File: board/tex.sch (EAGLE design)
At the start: 248 parts, among them K1 HLS8L-DC5V-S-C, K2 HLS8L-DC5V-S-C, K3 HLS8L-DC5V-S-C, K4 HLS8L-DC5V-S-C, Q47 FDD4141, U14 24LC32A, U15 OPTO-LTV817, U16 OPTO-LTV817, U17 OPTO-LTV817, U18 OPTO-LTV817, U19 RELAY-S108T02PTH, U2 RTC-DS1337S, U20 RELAY-S108T02PTH, U21 IO-HC4051, U5 AZ23C5V1, Y1 32.768KHz

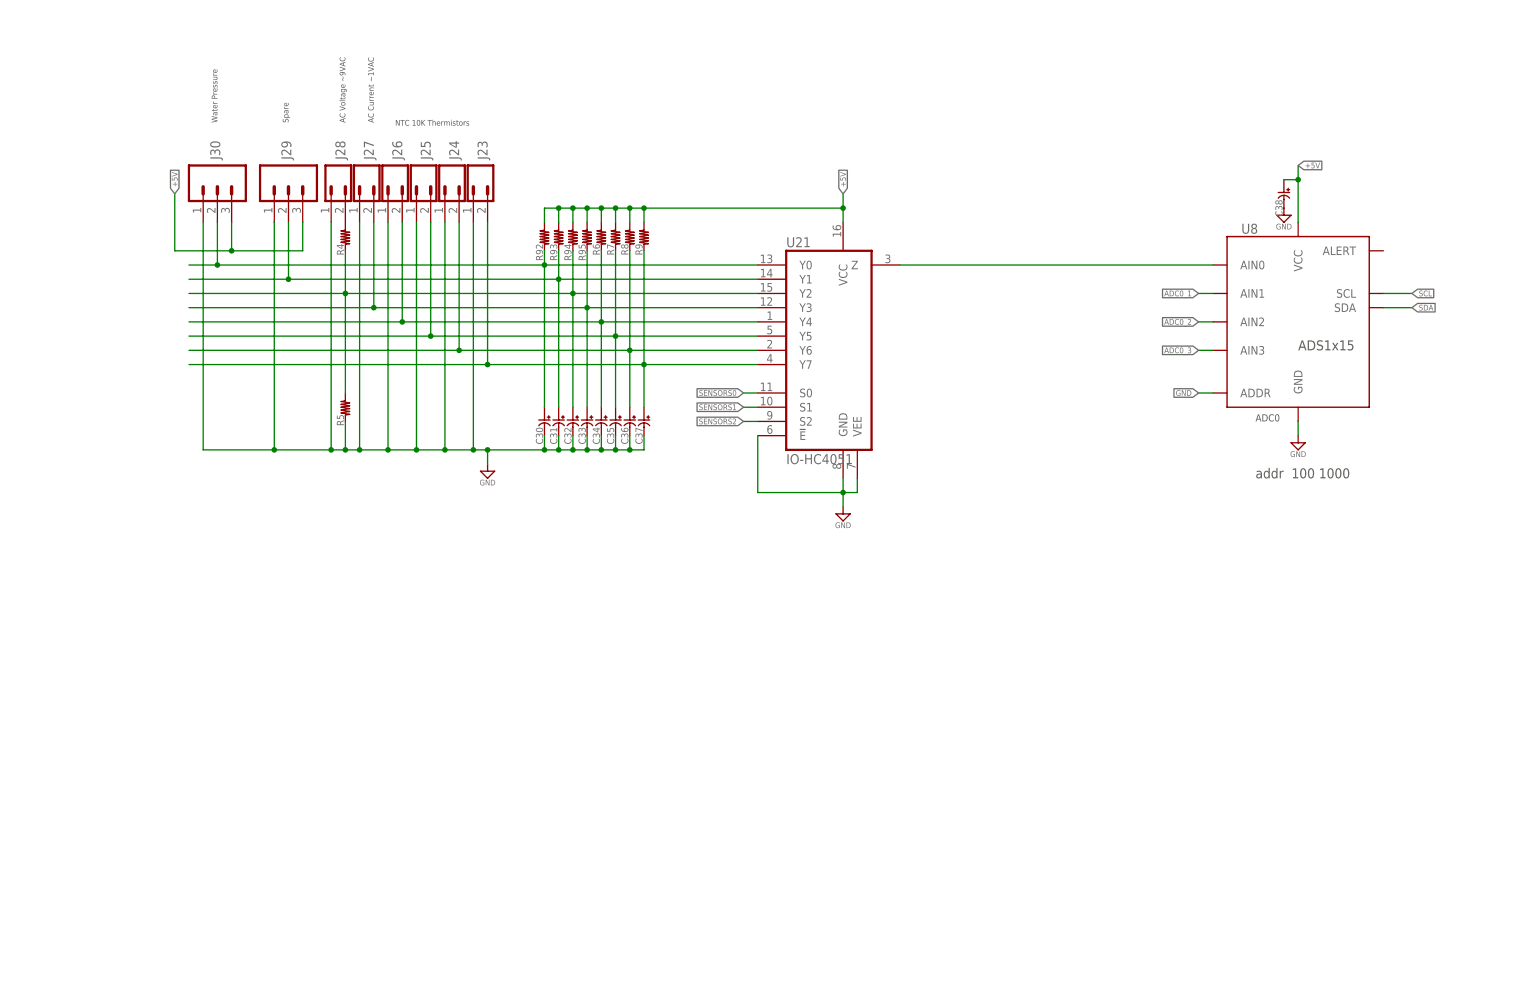
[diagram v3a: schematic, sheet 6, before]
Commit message: started routing changed rtc to MCP to have vbat
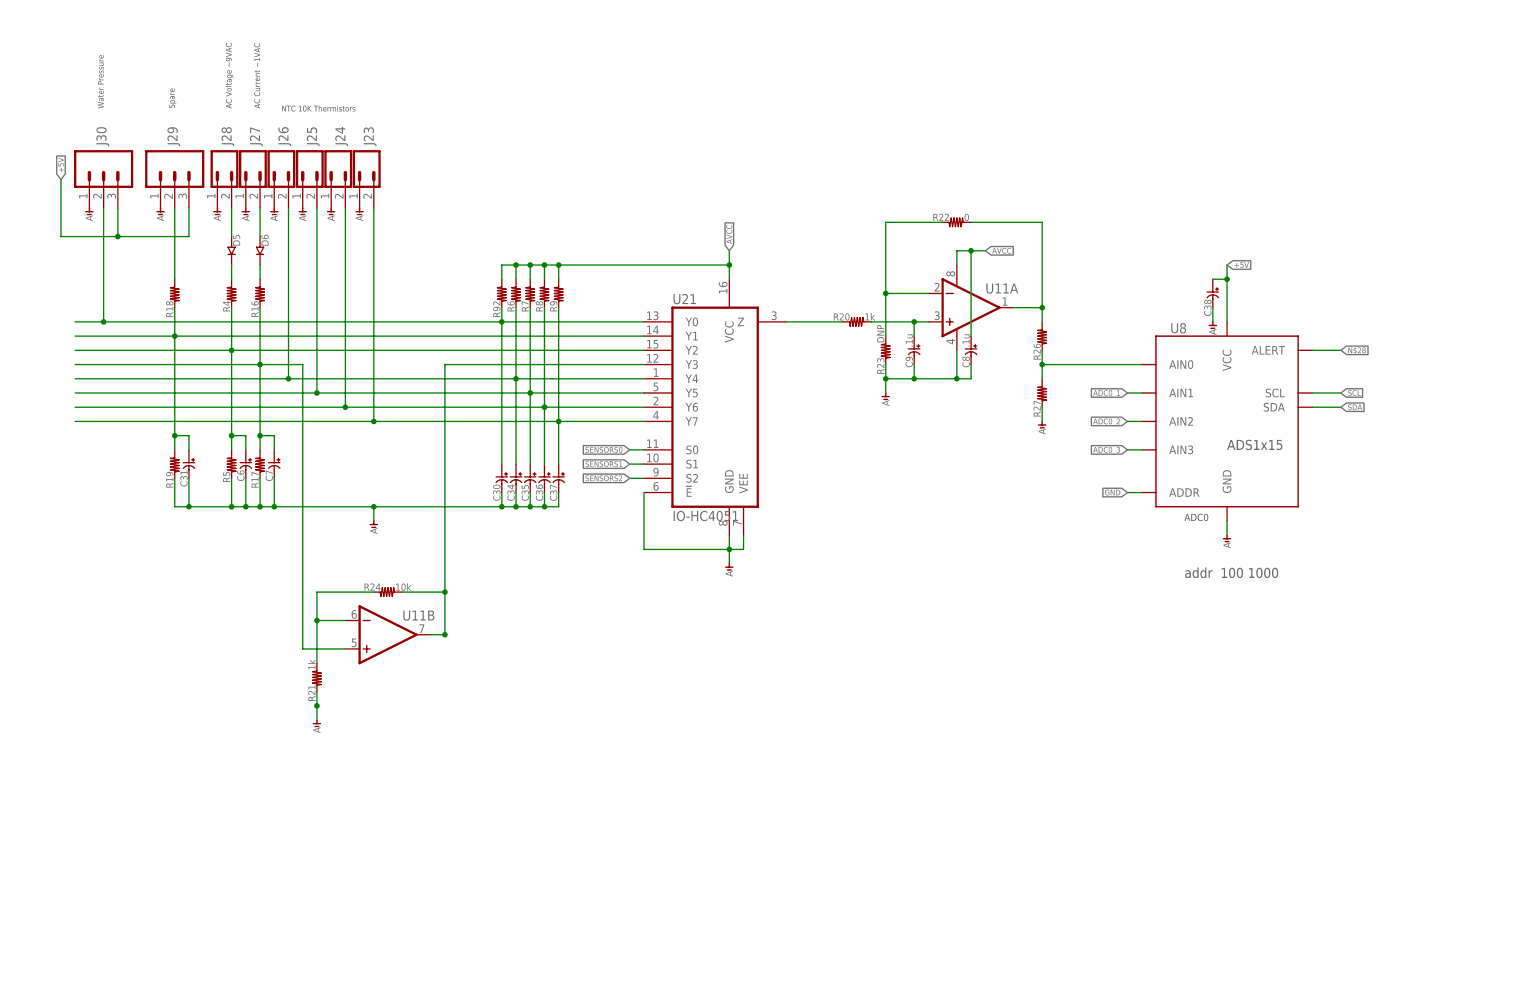
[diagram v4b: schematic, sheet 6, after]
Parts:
- removed C32, C33: (no value), holla:C-USC0603
- added B1: CONN-COINBATTERYHOLDER-20MM, holla:CONN-COINBATTERYHOLDER-20MM
- added C11, C12, C8, C9: .1u, holla:C-USC0603
- added C6, C7: (no value), holla:C-USC0603
- added D5, D6: (no value), holla:DIODE-0805
- added J18: (no value), holla:M04-0.1
- added R16, R17, R18, R19, R25, R26, R27: (no value), holla:R-US_R0603
- added R20, R21: 1k, holla:R-US_R0603
- added R22: 0, holla:R-US_R0603
- added R23: DNP, holla:R-US_R0603
- added R24: 10k, holla:R-US_R0603
- added U11: (no value), holla:AMP-OPAMP-DUAL-SO08
- R10: device rcl:R-US_R0402 -> holla:R-US_R0603
- R93, R94, R95: value (none) -> 120
- U2: value RTC-DS1337S -> (none); device holla:RTC-DS1337S -> holla:RTC-MCP7940N
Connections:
- net C_24IN renamed N$194
- removed net !RTC_INTA: U2.!INTA
- removed net !RTC_INTB: U2.SQW/!INTB
- removed net N$160: D28.C, D29.C, D30.C, D31.C, K1.V+, K2.V+, K3.V+, K4.V+, R85.2, R86.2, R87.2
- new net N$188: R22.2, R26.2, U11A.OUT
- new net N$189: R20.1, U21.Z
- new net N$190: R26.1, R27.2, U8.AIN0
- new net N$191: R24.2, U11B.OUT, U21.Y3
- new net N$192: R95.1, U2.MFP
- new net N$20: D5.A, J28.2
- new net N$25: D6.C, R16.2
- new net N$26: D6.A, J27.2
- new net N$27: J29.2, R18.2
- new net N$28: U8.ALERT
- new net N$38: R22.1, R23.2, U11A.-IN
- new net N$39: R21.2, R24.1, U11B.-IN
- new net N$55: C9.1, R20.2, U11A.+IN
- net +3V3: now also R93.2, R94.2
- net +5V: now also J18.2; no longer R6.2, R7.2, R8.2, R9.2, R92.2, R93.2, R94.2, U21.VCC
- net AGND: now also C15.2, C16.2, C17.2, C30.2, C31.2, C34.2, C35.2, C36.2, C37.2, C38.2, C6.2, C7.2, C8.2, C9.2, J23.1, J24.1, J25.1, J26.1, J27.1, J28.1, J29.1, J30.1, R17.1, R19.1, R21.1, R23.1, R25.2, R27.1, R5.1, U10A.V-, U11A.V-, U21.!E, U21.GND, U21.VEE, U8.GND
- net AVCC: now also C8.1, R6.2, R7.2, R8.2, R9.2, R92.2, U11A.V+, U21.VCC
- net GND: now also B1.-, C11.2, C12.2, J18.1, R10.2, R25.1; no longer C15.2, C16.2, C17.2, C30.2, C31.2, C32.2, C33.2, C34.2, C35.2, C36.2, C37.2, C38.2, J23.1, J24.1, J25.1, J26.1, J27.1, J28.1, J29.1, J30.1, R10.1, R5.1, U10A.V-, U2.GND, U21.!E, U21.GND, U21.VEE, U8.GND
- net N$118: now also B1.+1, U2.VBAT; no longer U21.Z, U8.AIN0
- net N$124: now also R18.1, R19.2; no longer J29.2, R93.1
- net N$130: now also C6.1; no longer C32.1, R94.1
- net N$138: now also C7.1, R16.1, R17.2, U11B.+IN; no longer C33.1, J27.2, R95.1, U21.Y3
- net N$172: now also D28.C, D29.C, D30.C, D31.C, K1.V+, K2.V+, K3.V+, K4.V+, R85.2, R86.2, R87.2
- net N$2: now also D5.C; no longer J28.2
- net N$3: now also C11.1
- net N$4: now also R10.1; no longer R10.2
- net N$5: now also C12.1
- net N$61: now also Q34.G
- net SCL: now also J18.3, R94.1
- net SDA: now also J18.4, R93.1
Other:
- note added: "120VAC"
- note added: "15A"
- note added: "16 channels"
- note added: "1VAC"
- note added: "9VAC"
- note added: "AGND not implemented, not high-performance design I2C Address Table 010 0000 I/O MCP23107 100 0000 VBATT Current Sense INA219 100 1000 ADC ADS1015 100 1100 TEMP LM75 110 0000 LED PCA9685 110 1111 RTC MCP7940 111 1000 Display SSD1306 Banggood"
- note added: "Batt"
- note added: "C-XFRM"
- note added: "HSADC"
- note added: "RPI I/O 3.3V Max VBATT, 5V, 3.3V available"
- note added: "RS485"
- note added: "UI SWITCH"
- note added: "XFRM"
- note added: "addr 110 1111"
- note added: "connect adc alert to rpi"
- note removed: "12x"
- note removed: "AGND not implemented, not high-performance design I2C Address Table 010 0000 I/O MCP23107 100 0000 VBATT Current Sense INA219 100 1000 ADC ADS1015 100 1100 TEMP LM75 110 0000 LED PCA9685 110 1000 RTC DS1337 111 1000 Display SSD1306 Banggood"
- note removed: "AMP"
- note removed: "Serial"
- note removed: "VCC +3.3V"
- note removed: "add current sense at the fuse level add I2C oled display add clamp to incoming voltage, motor spikes"
- note removed: "addr 110 1000"
- moved on the sheet: C1, C30, C31, C34, C35, C36, C37, C38, J23, J24, J25, J26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

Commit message: routing
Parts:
- removed D3: (no value), holla:LED-0603
- removed R14, R15, R3: (no value), holla:R-US_R0603
- removed S2, S4: (no value), holla:SWITCH-PUSHBUTTON-6MMX3.5MM
- added D0: (no value), holla:LED-0603
- added R0: (no value), holla:R-US_R0603
- renumbered S3 to S0
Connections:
- removed net DCMOTOR1ENCA: U15.4
- removed net DCMOTOR1ENCB: U16.4
- removed net DCMOTOR2ENCA: U17.4
- removed net DCMOTOR2ENCB: U18.4
- removed net N$10: U7.DI
- removed net N$106: PCB1.GPIO4
- removed net N$11: U7.RO
- removed net N$110: PCB1.GPIO18
- removed net N$112: PCB1.GPIO23
- removed net N$113: PCB1.GPIO24
- removed net N$115: PCB1.GPIO25
- removed net N$116: PCB1.GPIO8
- removed net N$117: PCB1.GPIO7
- removed net N$119: PCB1.GPIO12
- removed net N$12: U7.!RE
- removed net N$121: PCB1.GPIO16
- removed net N$122: PCB1.GPIO20
- removed net N$123: PCB1.GPIO21
- removed net N$125: PCB1.GPIO26
- removed net N$126: PCB1.GPIO19
- removed net N$127: PCB1.GPIO13
- removed net N$128: PCB1.GPIO6
- removed net N$129: PCB1.GPIO5
- removed net N$131: PCB1.GPIO11
- removed net N$132: PCB1.GPIO9
- removed net N$133: PCB1.GPIO10
- removed net N$134: PCB1.3V3@17
- removed net N$135: PCB1.GPIO22
- removed net N$136: PCB1.GPIO27
- removed net N$137: PCB1.GPIO17
- removed net N$19: U7.DE
- removed net N$21: R15.1, S1.2
- removed net N$22: R14.1, S2.2
- removed net N$23: R13.1, S0.2
- removed net N$24: R12.1, S4.2
- removed net N$28: U8.ALERT
- removed net N$31 (its old number): D3.A, R3.1
- removed net N$32: R1.2
- removed net N$33: R2.2
- removed net N$34: R3.2
- removed net STEPPER1DIR: Q38.G, R74.2
- removed net STEPPER1EN: Q37.G, R73.2
- removed net STEPPER1STEP: Q39.G, R75.2
- removed net STEPPER2DIR: Q41.G, R77.2
- removed net STEPPER2EN: Q40.G, R76.2
- removed net STEPPER2STEP: Q42.G, R78.2
- new net ADCALERT: PCB1.GPIO27, U8.ALERT
- new net D0: PCB1.GPIO9, R0.2
- new net D1: PCB1.GPIO11, R1.2
- new net D2: PCB1.GPIO8, R2.2
- new net DCMOTORAENCA: PCB1.GPIO24, U15.4
- new net DCMOTORAENCB: PCB1.GPIO23, U16.4
- new net DCMOTORBENCA: PCB1.GPIO7, U17.4
- new net DCMOTORBENCB: PCB1.GPIO25, U18.4
- new net N$29: D0.A, R0.1
- new net RXEN: PCB1.GPIO18, U7.!RE
- new net S0: PCB1.GPIO22, R13.1, S0.2
- new net S1: PCB1.GPIO10, R12.1, S1.2
- new net STEPPERADIR: PCB1.GPIO12, Q41.G, R77.2
- new net STEPPERAEN: PCB1.GPIO5, Q40.G, R76.2
- new net STEPPERASTEP: PCB1.GPIO6, Q42.G, R78.2
- new net STEPPERBDIR: PCB1.GPIO16, Q38.G, R74.2
- new net STEPPERBEN: PCB1.GPIO13, Q37.G, R73.2
- new net STEPPERBSTEP: PCB1.GPIO19, Q39.G, R75.2
- new net TXEN: PCB1.GPIO4, U7.DE
- net +3V3: now also PCB1.3V3@17; no longer R14.2, R15.2
- net GND: now also D0.C; no longer D3.C, S2.1, S4.1
- net INPUTINTERRUPT: now also PCB1.GPIO17
- net SENSORS0: now also PCB1.GPIO21
- net SENSORS1: now also PCB1.GPIO26
- net SENSORS2: now also PCB1.GPIO20
- net UART0_RX: now also U7.RO
- net UART0_TX: now also U7.DI
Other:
- note added: "connect adc alert to rpi does ina219 give the vbatt voltage? do something adc0_3"
- note removed: "connect adc alert to rpi"
- note removed: "put MAX13433E here"
- moved on the sheet: D1, D2, R1, R2, S1

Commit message: routing complete
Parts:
- added C10: (no value), holla:C-USC0603
- added R3: (no value), holla:R-US_R0603
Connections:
- net +5V: now also R3.1; no longer C38.1, U8.VCC
- net AGND: now also C10.2, U8.ADDR
- net AVCC: now also C10.1, C38.1, R3.2, U8.VCC
- net GND: no longer U8.ADDR
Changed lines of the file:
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@@
 <part name="R93" library="holla" deviceset="R" device="-US_R0603" value="120"/>
 <part name="R94" library="holla" deviceset="R" device="-US_R0603" value="120"/>
+<part name="R3" library="holla" deviceset="R" device="-US_R0603"/>
+<part name="C10" library="holla" deviceset="C" device="-USC0603"/>
+<part name="AGND21" library="holla" deviceset="AGND" device=""/>
 </parts>
 <sheets>
@@
 <instance part="R25" gate="G$1" x="76.2" y="101.6"/>
 <instance part="R10" gate="G$1" x="58.42" y="127" rot="R270"/>
+<instance part="R3" gate="G$1" x="88.9" y="101.6"/>
+<instance part="C10" gate="G$1" x="91.44" y="96.52"/>
+<instance part="AGND21" gate="VR1" x="91.44" y="91.44"/>
 </instances>
 <busses>
@@
 <label x="142.24" y="86.36" size="1.016" layer="95" rot="R90" xref="yes"/>
 </segment>
+<segment>
+<pinref part="R3" gate="G$1" pin="1"/>
+<wire x1="86.36" y1="101.6" x2="86.36" y2="104.14" width="0.1524" layer="91"/>
+<label x="86.36" y="104.14" size="1.016" layer="95" rot="R90" xref="yes"/>
+</segment>
 </net>
 <net name="N$101" class="0">
@@
 <wire x1="78.74" y1="101.6" x2="78.74" y2="99.06" width="0.1524" layer="91"/>
 </segment>
+<segment>
+<pinref part="AGND21" gate="VR1" pin="AGND"/>
+<pinref part="C10" gate="G$1" pin="2"/>
+<wire x1="91.44" y1="91.44" x2="91.44" y2="93.98" width="0.1524" layer="91"/>
+</segment>
 </net>
 <net name="N$194" class="0">
@@
 </segment>
 </net>
+<net name="AVCC" class="0">
+<segment>
+<pinref part="R3" gate="G$1" pin="2"/>
+<wire x1="91.44" y1="101.6" x2="91.44" y2="104.14" width="0.1524" layer="91"/>
+<label x="91.44" y="104.14" size="1.016" layer="95" rot="R90" xref="yes"/>
+<pinref part="C10" gate="G$1" pin="1"/>
+<wire x1="91.44" y1="101.6" x2="91.44" y2="99.06" width="0.1524" layer="91"/>
+<junction x="91.44" y="101.6"/>
+</segment>
+</net>
 </nets>
 </sheet>
@@
 <instance part="AGND4" gate="VR1" x="187.96" y="137.16"/>
 <instance part="AGND5" gate="VR1" x="218.44" y="154.94"/>
-<instance part="AGND6" gate="VR1" x="220.98" y="116.84"/>
+<instance part="AGND6" gate="VR1" x="220.98" y="114.3"/>
 <instance part="AGND8" gate="VR1" x="68.58" y="119.38"/>
 <instance part="AGND10" gate="VR1" x="17.78" y="175.26"/>
@@
 </busses>
 <nets>
-<net name="GND" class="0">
-<segment>
-<pinref part="U8" gate="G$1" pin="ADDR"/>
-<wire x1="205.74" y1="124.46" x2="198.12" y2="124.46" width="0.1524" layer="91"/>
-<label x="198.12" y="124.46" size="1.016" layer="95" rot="R180" xref="yes"/>
-</segment>
-</net>
 <net name="+5V" class="0">
 <segment>
@@
 <label x="12.7" y="180.34" size="1.016" layer="95" rot="R90" xref="yes"/>
 </segment>
-<segment>
-<pinref part="U8" gate="G$1" pin="VCC"/>
-<wire x1="220.98" y1="154.94" x2="220.98" y2="162.56" width="0.1524" layer="91"/>
-<label x="220.98" y="165.1" size="1.016" layer="95" xref="yes"/>
-<pinref part="C38" gate="G$1" pin="1"/>
-<wire x1="220.98" y1="162.56" x2="220.98" y2="165.1" width="0.1524" layer="91"/>
-<wire x1="218.44" y1="162.56" x2="220.98" y2="162.56" width="0.1524" layer="91"/>
-<junction x="220.98" y="162.56"/>
-</segment>
 </net>
 <net name="N$120" class="0">
@@
 <pinref part="U8" gate="G$1" pin="GND"/>
 <pinref part="AGND6" gate="VR1" pin="AGND"/>
+<wire x1="220.98" y1="114.3" x2="220.98" y2="116.84" width="0.1524" layer="91"/>
 <wire x1="220.98" y1="116.84" x2="220.98" y2="119.38" width="0.1524" layer="91"/>
+<wire x1="220.98" y1="116.84" x2="203.2" y2="116.84" width="0.1524" layer="91"/>
+<wire x1="203.2" y1="116.84" x2="203.2" y2="124.46" width="0.1524" layer="91"/>
+<pinref part="U8" gate="G$1" pin="ADDR"/>
+<wire x1="203.2" y1="124.46" x2="205.74" y2="124.46" width="0.1524" layer="91"/>
+<junction x="220.98" y="116.84"/>
 </segment>
 <segment>
@@
 <junction x="101.6" y="165.1"/>
 </segment>
+<segment>
+<pinref part="U8" gate="G$1" pin="VCC"/>
+<wire x1="220.98" y1="154.94" x2="220.98" y2="162.56" width="0.1524" layer="91"/>
+<label x="220.98" y="165.1" size="1.016" layer="95" rot="R90" xref="yes"/>
+<pinref part="C38" gate="G$1" pin="1"/>
+<wire x1="220.98" y1="162.56" x2="220.98" y2="165.1" width="0.1524" layer="91"/>
+<wire x1="218.44" y1="162.56" x2="220.98" y2="162.56" width="0.1524" layer="91"/>
+<junction x="220.98" y="162.56"/>
+</segment>
 </net>
